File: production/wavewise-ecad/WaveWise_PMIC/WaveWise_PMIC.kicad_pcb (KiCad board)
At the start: 4 copper layers, 49 parts, among them IC1 LV14360PDDAR, J1 24V output, J10 5031590200, J11 5031590200, J12 Regulated 48V Input, J2 Inverter Inputs, J3 Conn_01x03_Pin, J4 Conn_01x04_Pin, J5 5031590400, J6 5031590400, J7 5V output, J8 5031590800, J9 5031590300, K1 Relay_SPST-NO, Q2 2N2219, U1 Raspberry Pi Pico, U2 Pololu_DRV8711_Motor_Driver, U4 LM2576HVS-5.0_NOPB

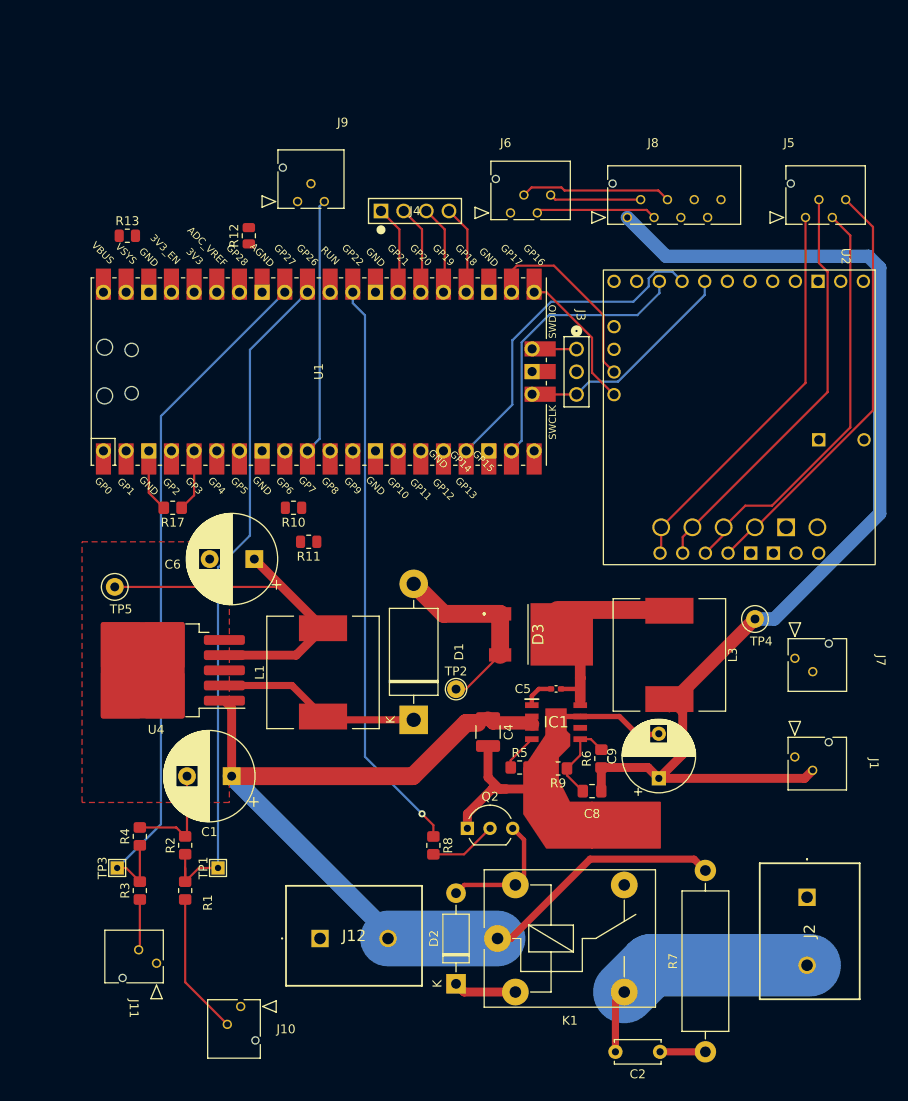
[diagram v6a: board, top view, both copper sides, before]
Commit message: Completed all connections and added mounting holes
Needs some review with the DRC tool
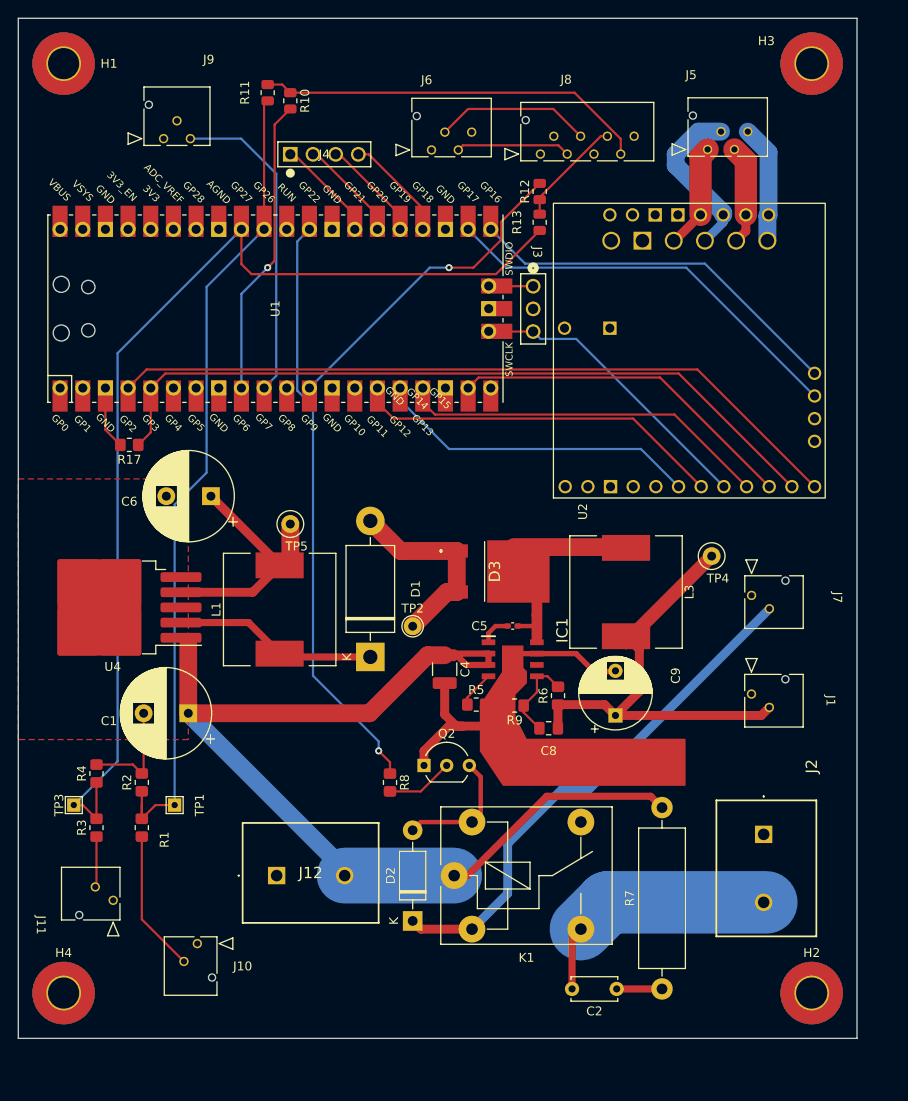
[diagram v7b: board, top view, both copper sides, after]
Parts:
- added H1: MountingHole, MountingHole:MountingHole_3.5mm_Pad_TopBottom, F.Cu at (78.7, 53.3)
- added H2: MountingHole, MountingHole:MountingHole_3.5mm_Pad_TopBottom, F.Cu at (162.6, 157.5)
- added H3: MountingHole, MountingHole:MountingHole_3.5mm_Pad_TopBottom, F.Cu at (162.6, 53.3)
- added H4: MountingHole, MountingHole:MountingHole_3.5mm_Pad_TopBottom, F.Cu at (78.7, 157.5)
- moved U2 51.2 mm to (131.2, 104.7), turned to 90 degrees
- moved R11 50.5 mm to (101.6, 56.6), turned to -90 degrees
- moved R13 46.2 mm to (132.1, 71.1), turned to -90 degrees
- moved R10 45.6 mm to (104.1, 57.5), turned to -90 degrees
- moved R12 33.0 mm to (132.1, 67.7)
- moved TP5 20.9 mm to (104.1, 104.9)
- moved J9 16.6 mm to (89.9, 61.7)
- moved J5 13.4 mm to (150.9, 63.0)
- moved J8 12.1 mm to (132.2, 63.5)
- moved J4 12.0 mm to (104.1, 63.5)
- moved J6 11.3 mm to (120.0, 63.0)
- moved R9 8.56 mm to (129.3, 125.3)
- moved C8 8.56 mm to (133.1, 127.8)
- moved C9 8.56 mm to (140.6, 126.4)
- moved D1 8.56 mm to (113.1, 119.8)
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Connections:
- J5 pad 1: /Connectors/BOUT2 -> /Connectors/AOUT1
- J5 pad 2: /Connectors/BOUT1 -> /Connectors/AOUT2
- J5 pad 3: /Connectors/AOUT2 -> /Connectors/BOUT1
- J5 pad 4: /Connectors/AOUT1 -> /Connectors/BOUT2
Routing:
- net batt_sense: track 0.00 -> 43.8 mm
- net /Panel_Sense: track 79.5 -> 119.3 mm
- net /panel_sense_DIO: track 0.00 -> 36.5 mm, vias 0 -> 1
- net /Connectors/AOUT1: track 47.7 -> 11.9 mm
- net /Connectors/BOUT1: track 46.7 -> 11.2 mm
- net /DIO_BatterySense: track 0.00 -> 33.5 mm, vias 0 -> 1
- net /Connectors/BOUT2: track 44.4 -> 13.2 mm
- net +5V: track 173.0 -> 143.8 mm
- net /Connectors/AOUT2: track 46.9 -> 18.9 mm
- net /BEMF: track 16.0 -> 43.0 mm
- net /MOTOR_FLT: track 57.5 -> 83.2 mm
- net /STALL: track 22.1 -> 46.6 mm
- net /MOTOR_RESET: track 64.4 -> 84.7 mm
- net /BATT_SENS: track 77.6 -> 92.1 mm
- net +24V: track 130.9 -> 117.5 mm
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- added copper zone on In1.Cu, net +48V
- added copper zone on In1.Cu, net +5V
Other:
- board outline added: 94 x 114.3 mm

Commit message: Prelim board layout
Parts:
- removed H3: MountingHole, MountingHole:MountingHole_3.5mm_Pad_TopBottom
- removed J1: 24V output, Unchecked:2pinmolex
- removed J12: Regulated 48V Input, Unchecked:1731721
- removed J4: Conn_01x04_Pin, Unchecked:61300411121
- removed J7: 5V output, Unchecked:2pinmolex
- removed TP1, TP3: TestPoint, TestPoint:TestPoint_THTPad_1.5x1.5mm_Drill0.7mm
- removed TP2: TestPoint, TestPoint:TestPoint_THTPad_D2.0mm_Drill1.0mm
- removed TP4: 24V TP, TestPoint:TestPoint_Loop_D1.80mm_Drill1.0mm_Beaded
- removed TP5: 5V TP, TestPoint:TestPoint_Loop_D1.80mm_Drill1.0mm_Beaded
- added 24V_1: 24V TP, TestPoint:TestPoint_Loop_D1.80mm_Drill1.0mm_Beaded, F.Cu at (63.5, 115.1)
- added 3V1: TestPoint, TestPoint:TestPoint_Pad_D1.5mm, F.Cu at (91.2, 66.0)
- added 5V1: 5V TP, TestPoint:TestPoint_Loop_D1.80mm_Drill1.0mm_Beaded, F.Cu at (128.8, 57.7)
- added BatteryV1: TestPoint, TestPoint:TestPoint_THTPad_1.5x1.5mm_Drill0.7mm, F.Cu at (111.8, 53.8)
- added GND1: TestPoint, TestPoint:TestPoint_THTPad_D2.0mm_Drill1.0mm, F.Cu at (96.8, 114.0)
- added HE1: MountingHole, MountingHole:MountingHole_3.2mm_M3_ISO7380_Pad, F.Cu at (55.1, 125.5)
- added J13: Screw_Terminal_01x03, Unchecked:CONN_1731734_PXC, F.Cu at (133.1, 95.6)
- added PanelV1: TestPoint, TestPoint:TestPoint_THTPad_1.5x1.5mm_Drill0.7mm, F.Cu at (93.2, 55.1)
- added R14: 0, Resistor_SMD:R_0805_2012Metric, F.Cu at (93.7, 61.0)
- added R15: 0, Resistor_SMD:R_0805_2012Metric, F.Cu at (56.9, 97.3)
- added R16: 0, Resistor_SMD:R_0805_2012Metric, F.Cu at (55.1, 80.7)
- added R18: 0, Resistor_SMD:R_0805_2012Metric, F.Cu at (54.4, 97.3)
- added R19: 0, Resistor_SMD:R_0805_2012Metric, F.Cu at (52.9, 80.8)
- added R20: 0, Resistor_SMD:R_0805_2012Metric, F.Cu at (53.1, 60.7)
- added R21: 0, Resistor_SMD:R_0805_2012Metric, F.Cu at (129.0, 52.8)
- added R22: 0, Resistor_SMD:R_0805_2012Metric, F.Cu at (60.7, 127.5)
- added R23: 0, Resistor_SMD:R_0805_2012Metric, F.Cu at (136.0, 120.4)
- added R24: 0, Resistor_SMD:R_0805_2012Metric, F.Cu at (93.7, 64.8)
- added R25: 0, Resistor_SMD:R_0805_2012Metric, F.Cu at (62.5, 105.7)
- added R26: 0, Resistor_SMD:R_0805_2012Metric, F.Cu at (111.5, 93.7)
- C5: footprint Capacitor_SMD:C_0402_1005Metric_Pad0.74x0.62mm_HandSolder -> Capacitor_SMD:C_0805_2012Metric_Pad1.18x1.45mm_HandSolder
- D3: footprint SBR10200CTL-13:ZLDO1117K50TC -> Unchecked:TO-252DPAK_DIO
- H1, H2, H4: footprint MountingHole:MountingHole_3.5mm_Pad_TopBottom -> MountingHole:MountingHole_3.2mm_M3_ISO7380_Pad
- IC1: footprint LV14360PDDAR:SOIC127P600X170-9N -> Package_SO:SOIC-8-1EP_3.9x4.9mm_P1.27mm_EP2.41x3.3mm_ThermalVias
- J2: value Inverter Inputs -> Conn_01x06_Pin; footprint Unchecked:1731721 -> Unchecked:61300611121
- J5, J6: footprint Footprints:4pinmolex -> Unchecked:4pinmolex
- J8: footprint Footprints:8pinmolex -> Unchecked:8pinmolex
- K1: value Relay_SPST-NO -> AWHSH105D00G; footprint Relay_THT:Relay_SPDT_Finder_36.11 -> Unchecked:AWHSH105D00G
- U4: footprint Package_TO_SOT_SMD:TO-263-5_TabPin3 -> Package_TO_SOT_SMD:TO-263-5_TabPin6
- moved J2 114.8 mm to (58.7, 80.8), turned to 90 degrees
- moved H2 105.7 mm to (135.1, 55.4)
- moved J10 97.5 mm to (119.4, 57.9), turned to 0 degrees
- moved J11 91.1 mm to (102.6, 57.9), turned to 0 degrees
- moved J8 89.6 mm to (58.1, 113.8), turned to 90 degrees
- moved R3 85.9 mm to (97.3, 54.4), turned to -90 degrees
- moved R1 85.1 mm to (112.8, 57.7)
- moved C9 80.9 mm to (59.8, 121.7), turned to 0 degrees
- moved R2 79.6 mm to (110.5, 57.7)
- moved R13 79.0 mm to (62.4, 108.2), turned to 0 degrees
- moved R4 76.5 mm to (96.3, 57.7), turned to 0 degrees
- moved R12 72.1 mm to (60.2, 62.7), turned to 0 degrees
- moved J6 68.0 mm to (58.1, 91.4), turned to 90 degrees
- moved R6 67.7 mm to (67.3, 113.3)
- moved R7 67.6 mm to (124.2, 93.0), turned to -90 degrees
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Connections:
- net /Connectors/AOUT1 renamed /AOUT1
- net /Connectors/AOUT2 renamed /AOUT2
- net /Connectors/BOUT1 renamed /BOUT1
- net /Connectors/BOUT2 renamed /BOUT2
- C2 pad 2: /Connectors/Inverter_Input -> /Inverter_Input
- H1 pad 1: (no net) -> Net-(H1-Pad1)
- H2 pad 1: (no net) -> Net-(H2-Pad1)
- H4 pad 1: (no net) -> Net-(H4-Pad1)
- J2 pad 1: GND -> /Connectors/GPIO4
- J2 pad 2: /Connectors/Inverter_Input -> /Connectors/GPIO3
- J3 pad 1: /Connectors/DIO -> /Connectors/SWCLK
- J3 pad 3: /CLK -> /Connectors/SWDIO
- J6 pad 2: /Connectors/rockblock_RX -> /Connectors/rockblock_TX
- J6 pad 3: /Connectors/rockblock_TX -> /Connectors/rockblock_RX
- J8 pad 3: /Connectors/rockblock_TX -> /Connectors/SICO_TX
- J8 pad 4: /Connectors/rockblock_RX -> /Connectors/SICO_RX
- R1 pad 2: /BATT_SENS -> /Connectors/Batt V Sense
- R10 pad 2: /DIO_BatterySense -> /Connectors/BATT_SENSE_DIO
- R11 pad 2: /BATT_SENS -> /Connectors/Batt V Sense
- R12 pad 2: /panel_sense_DIO -> /Connectors/PANEL_SENSE_DIO
- R13 pad 2: /Panel_Sense -> /Connectors/Panel V Sense
- R17 pad 1: /MOTOR_RESET -> /PICO (BICO)/MOTOR_RESET
- R2 pad 1: /BATT_SENS -> /Connectors/Batt V Sense
- R3 pad 2: /Panel_Sense -> /Connectors/Panel V Sense
- R4 pad 1: /Panel_Sense -> /Connectors/Panel V Sense
- R8 pad 1: /PUMP_CTL -> /PICO (BICO)/PUMP_CTRL
- U1 pad 1: /PICO (BICO)/B_TX -> /Connectors/BICO_UART_TX
- U1 pad 10: /Connectors/PWM_Servo -> /Connectors/GPIO2
- U1 pad 11: unconnected-(U1-GPIO8-Pad11) -> /Connectors/GPIO3
- U1 pad 12: /panel_sense_DIO -> /Connectors/GPIO4
- U1 pad 14: /PICO (BICO)/SCK -> unconnected-(U1-GPIO10-Pad14)
- U1 pad 15: /PICO (BICO)/MOSI1 -> unconnected-(U1-GPIO11-Pad15)
- U1 pad 16: /PICO (BICO)/MISO1 -> unconnected-(U1-GPIO12-Pad16)
- U1 pad 17: /PICO (BICO)/SCS -> /PICO (BICO)/MOTOR_SLP
- U1 pad 19: /~SLP -> /PICO (BICO)/MOTOR_RESET
- U1 pad 2: /PICO (BICO)/B_RX -> /Connectors/BICO_UART_RX
- U1 pad 20: unconnected-(U1-GPIO15-Pad20) -> /PICO (BICO)/MOTOR_FLT
- U1 pad 21: /BEMF -> /PICO (BICO)/MOTOR_SPI0_RX
- U1 pad 22: /STALL -> /PICO (BICO)/MOTOR_SPI0_CSn
- U1 pad 24: /GPIO1 -> /PICO (BICO)/MOTOR_SPI0_SCK
- U1 pad 25: /GPIO2 -> /PICO (BICO)/MOTOR_SPI0_TX
- U1 pad 26: /GPIO3 -> /PICO (BICO)/MOTOR_DIR/AIN2
- U1 pad 27: /GPIO4 -> /PICO (BICO)/MOTOR_STEP/AIN1
- U1 pad 29: /PUMP_CTL -> /PICO (BICO)/MOTOR_STALL
- U1 pad 31: /BATT_SENS -> /PICO (BICO)/MOTOR_BEMF
- U1 pad 32: /Panel_Sense -> /Connectors/Batt V Sense
- U1 pad 33: unconnected-(U1-AGND-Pad33) -> GND
- U1 pad 34: unconnected-(U1-GPIO28_ADC2-Pad34) -> /Connectors/Panel V Sense
- U1 pad 36: unconnected-(U1-3V3-Pad36) -> +3.3V
- U1 pad 4: /MOTOR_FLT -> /Connectors/BATT_SENSE_DIO
- U1 pad 41: /CLK -> /Connectors/SWCLK
- U1 pad 43: /Connectors/DIO -> /Connectors/SWDIO
- U1 pad 5: /MOTOR_RESET -> /Connectors/PANEL_SENSE_DIO
- U1 pad 6: unconnected-(U1-GPIO4-Pad6) -> /Connectors/PWM_Servo
- U1 pad 7: unconnected-(U1-GPIO5-Pad7) -> /PICO (BICO)/PUMP_CTRL
- U1 pad 9: /DIO_BatterySense -> /Connectors/GPIO1
- U2 pad 10: /MOTOR_FLT -> /PICO (BICO)/MOTOR_FLT
- U2 pad 11: /MOTOR_RESET -> /PICO (BICO)/MOTOR_RESET
- U2 pad 12: /~SLP -> /PICO (BICO)/MOTOR_SLP
- U2 pad 13: /PICO (BICO)/SCS -> /PICO (BICO)/MOTOR_SPI0_CSn
- U2 pad 14: /CLK -> /PICO (BICO)/MOTOR_SPI0_SCK
- U2 pad 15: /PICO (BICO)/MOSI1 -> /PICO (BICO)/MOTOR_SPI0_TX
- U2 pad 16: /PICO (BICO)/MISO1 -> /PICO (BICO)/MOTOR_SPI0_RX
- U2 pad 17: unconnected-(U2-DIR-Pad17) -> /PICO (BICO)/MOTOR_DIR/AIN2
- U2 pad 18: unconnected-(U2-STEP-Pad18) -> /PICO (BICO)/MOTOR_STEP/AIN1
- U2 pad 19: unconnected-(U2-ICREF-Pad19) -> /Pneumatic Control/ICREF
- U2 pad 6: /BEMF -> /PICO (BICO)/MOTOR_BEMF
- U2 pad 7: /STALL -> /PICO (BICO)/MOTOR_STALL
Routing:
- net /Panel_Sense: track 119.3 -> 0.00 mm
- net +48V: track 116.6 -> 7.59 mm, vias 0 -> 1
- net +24V: track 117.5 -> 8.71 mm, vias 0 -> 1
- net +5V: track 143.8 -> 38.5 mm, vias 0 -> 1
- net /Connectors/Batt V Sense: track 0.00 -> 92.2 mm
- net /BATT_SENS: track 92.1 -> 0.00 mm
- net /MOTOR_RESET: track 84.7 -> 0.00 mm
- net /MOTOR_FLT: track 83.2 -> 0.00 mm
- net /Connectors/Panel V Sense: track 0.00 -> 81.7 mm
- net Net-(J13-Pin_2): track 0.00 -> 81.4 mm, vias 0 -> 2
- net /PUMP_CTL: track 65.9 -> 0.00 mm, vias 1 -> 0
- net /PICO (BICO)/PUMP_CTRL: track 0.00 -> 52.8 mm, vias 0 -> 1
- net /Connectors/Inverter_Input: track 50.9 -> 0.00 mm
- net /STALL: track 46.6 -> 0.00 mm
- net /BEMF: track 43.0 -> 0.00 mm
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- added copper zone on F.Cu, net +24V
- added copper zone on In1.Cu, net +24V
- added copper zone on F.Cu, net +48V
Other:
- board size 94 x 114.3 mm -> 88.9 x 80 mm
